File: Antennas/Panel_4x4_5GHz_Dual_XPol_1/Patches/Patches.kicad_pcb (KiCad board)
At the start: 2 copper layers, 186 x 226 mm, 92 parts

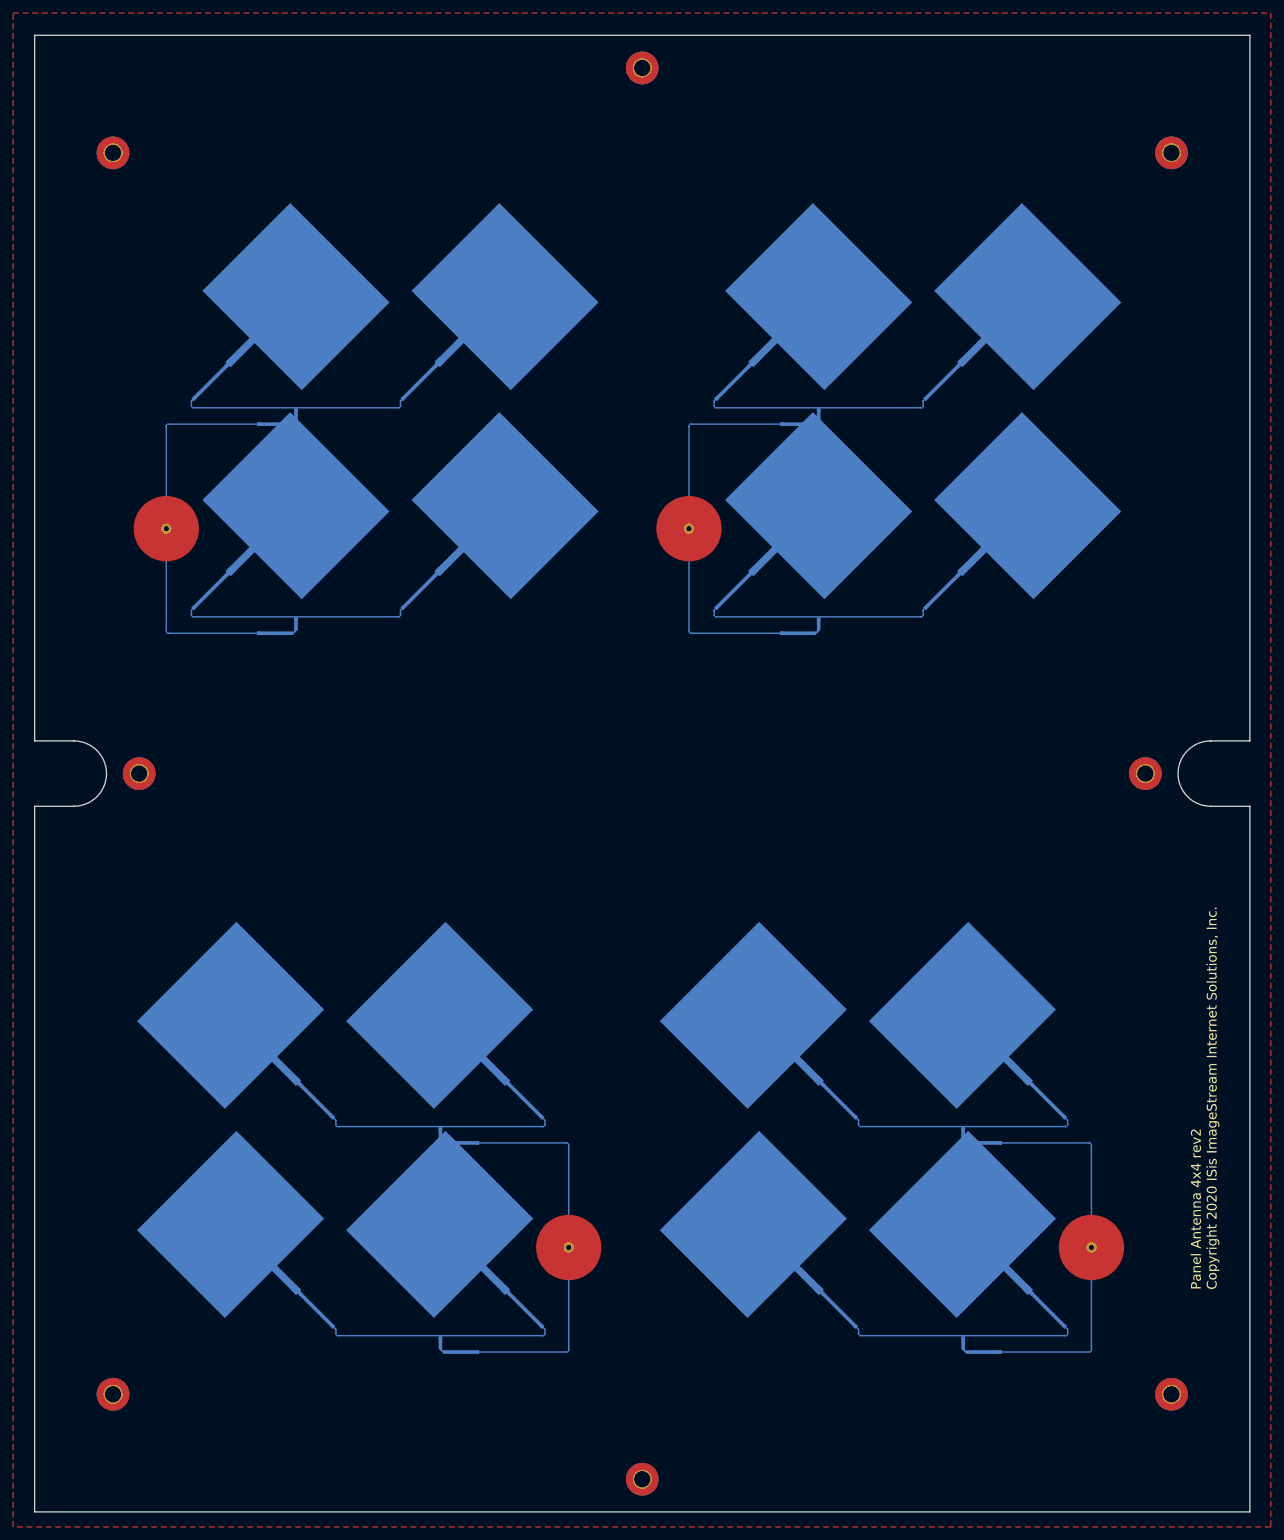
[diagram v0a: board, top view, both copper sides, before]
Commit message: Placed an order with JLCPCB for the Tighter 4pol version and the "Dual XPol" which actually was aperture coupled.
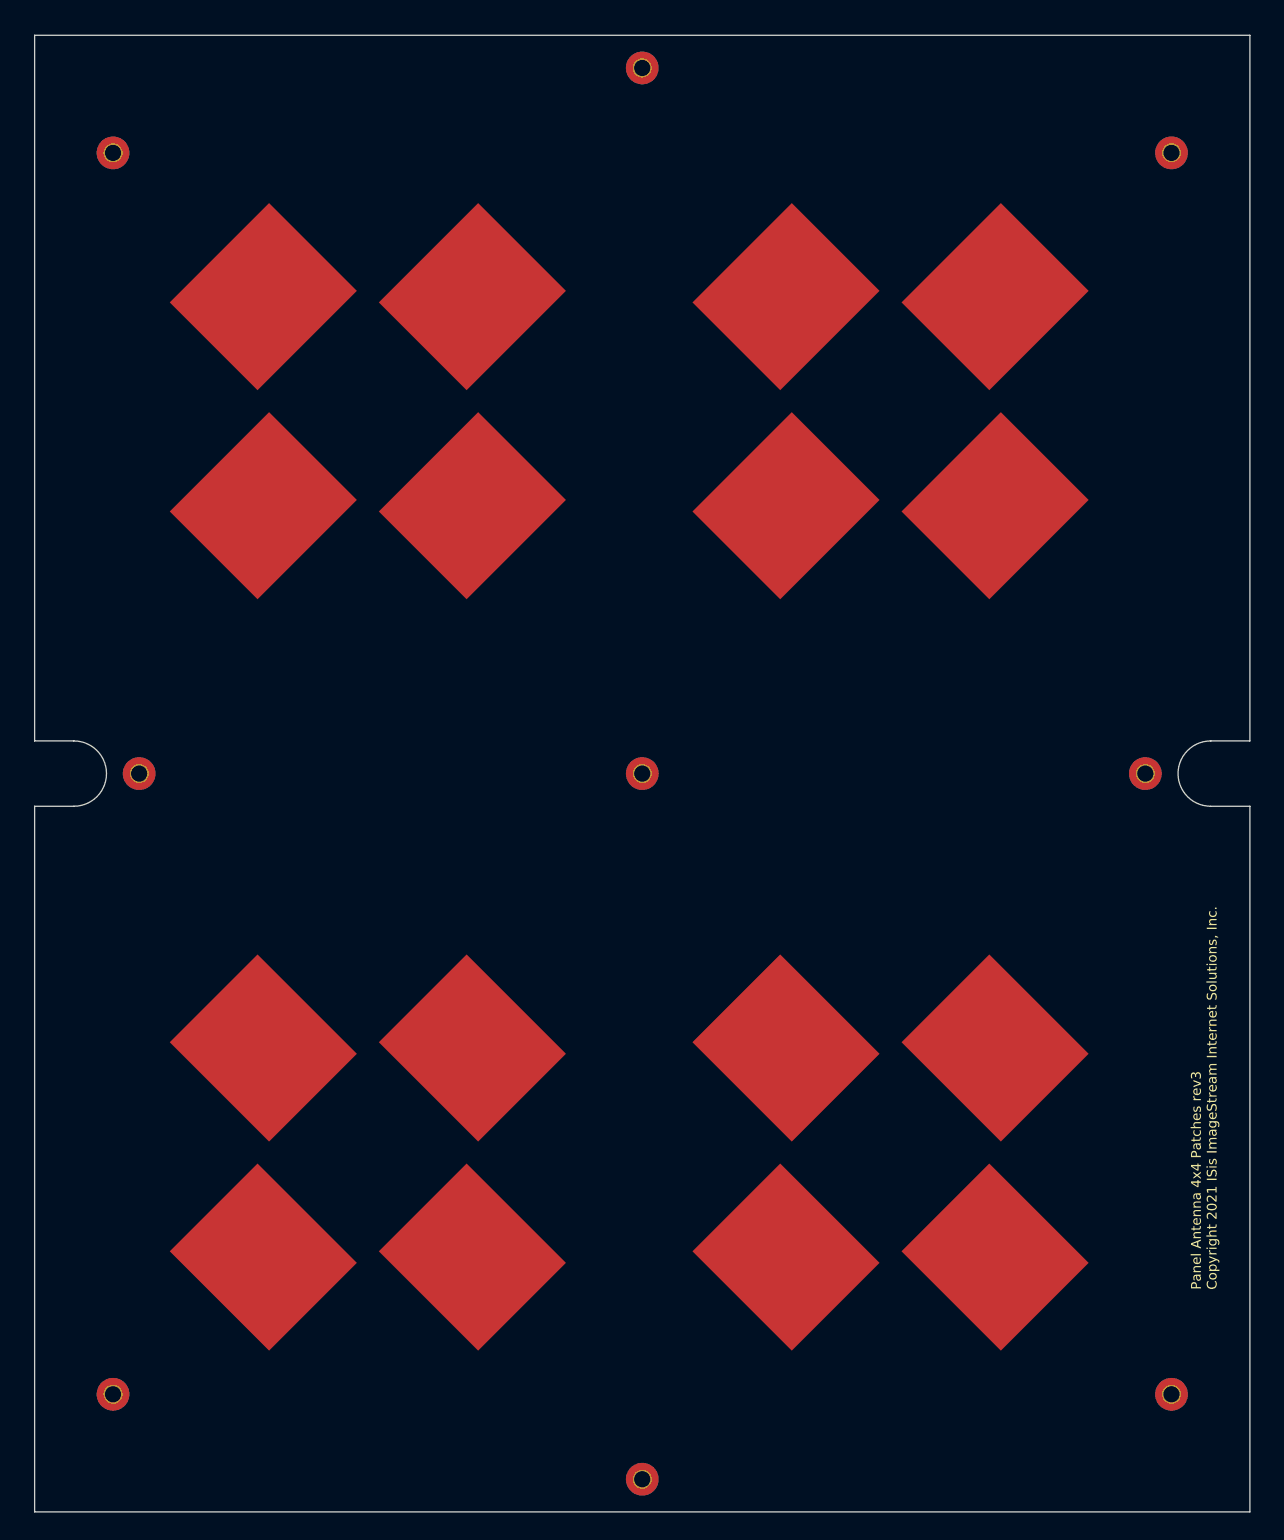
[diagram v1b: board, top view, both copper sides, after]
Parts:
- removed AE5 (x16): Antenna, Scott-RF-JLCPCB-600um7628-2layer:Feed_5.5_Linear_ApertureCoupled
- removed Feed1 (x4): Feed1, Scott:Flat_Ant_Hole
- removed the REF** at (78.1, 199.0)
- removed the REF** at (158.1, 167.0)
- removed the REF** at (40.0, 72.0)
- removed the REF** at (142.0, 150.0)
- removed the REF** at (104.0, 89.0)
- removed the REF** at (72.0, 40.0)
- removed the REF** at (142.1, 201.5)
- removed the REF** at (109.4, 82.6)
- removed the REF** at (152.6, 160.6)
- removed the REF** at (40.0, 59.5)
- removed the REF** at (56.0, 89.0)
- removed the REF** at (120.0, 72.0)
- removed the REF** at (24.0, 89.0)
- removed the REF** at (30.0, 182.0)
- removed the REF** at (142.1, 169.5)
- removed the REF** at (100.2, 91.5)
- removed the REF** at (40.6, 160.6)
- removed the REF** at (29.4, 50.6)
- removed the REF** at (126.1, 199.0)
- removed the REF** at (24.0, 57.0)
- removed the REF** at (62.0, 150.0)
- removed the REF** at (120.6, 160.6)
- removed the REF** at (161.7, 201.5)
- removed the REF** at (110.0, 182.0)
- removed the REF** at (40.0, 91.5)
- removed the REF** at (152.0, 40.0)
- removed the REF** at (62.0, 182.0)
- removed the REF** at (46.1, 199.0)
- removed the REF** at (161.7, 169.5)
- removed the REF** at (126.1, 167.0)
- removed the REF** at (40.0, 40.0)
- removed the REF** at (100.2, 59.5)
- removed the REF** at (81.7, 169.5)
- removed the REF** at (110.0, 150.0)
- removed the REF** at (120.0, 59.5)
- removed the REF** at (81.7, 201.5)
- removed the REF** at (30.0, 150.0)
- removed the REF** at (56.0, 57.0)
- removed the REF** at (20.2, 91.5)
- removed the REF** at (136.0, 57.0)
- removed the REF** at (109.4, 50.6)
- removed the REF** at (136.0, 89.0)
- removed the REF** at (152.6, 192.6)
- removed the REF** at (62.1, 169.5)
- removed the REF** at (104.0, 57.0)
- removed the REF** at (40.6, 192.6)
- removed the REF** at (141.4, 50.6)
- removed the REF** at (120.0, 40.0)
- removed the REF** at (120.0, 91.5)
- removed the REF** at (152.0, 72.0)
- removed the REF** at (61.4, 50.6)
- removed the REF** at (78.1, 167.0)
- removed the REF** at (72.6, 192.6)
- removed the REF** at (142.0, 182.0)
- removed the REF** at (72.0, 72.0)
- removed the REF** at (62.1, 201.5)
- removed the REF** at (141.4, 82.6)
- removed the REF** at (46.1, 167.0)
- removed the REF** at (29.4, 82.6)
- removed the REF** at (20.2, 59.5)
- removed the REF** at (72.6, 160.6)
- removed the REF** at (61.4, 82.6)
- removed the REF** at (158.1, 199.0)
- removed the REF** at (120.6, 192.6)
- added H11: Mounting Hole, MountingHole:MountingHole_2.5mm_Pad_TopBottom, F.Cu at (93.0, 113.0)
- added REF**: Patch_5.5_Linear_ApertureCoupled, Scott-RF-JLCPCB-600um7628-2layer:Patch_5.5_Linear_ApertureCoupled, F.Cu at (115.0, 187.0)
- added REF**: Patch_5.5_Linear_ApertureCoupled, Scott-RF-JLCPCB-600um7628-2layer:Patch_5.5_Linear_ApertureCoupled, F.Cu at (147.0, 187.0)
- added REF**: Patch_5.5_Linear_ApertureCoupled, Scott-RF-JLCPCB-600um7628-2layer:Patch_5.5_Linear_ApertureCoupled, F.Cu at (35.0, 155.0)
- added REF**: Patch_5.5_Linear_ApertureCoupled, Scott-RF-JLCPCB-600um7628-2layer:Patch_5.5_Linear_ApertureCoupled, F.Cu at (115.0, 72.0)
- added REF**: Patch_5.5_Linear_ApertureCoupled, Scott-RF-JLCPCB-600um7628-2layer:Patch_5.5_Linear_ApertureCoupled, F.Cu at (147.0, 40.0)
- added REF**: Patch_5.5_Linear_ApertureCoupled, Scott-RF-JLCPCB-600um7628-2layer:Patch_5.5_Linear_ApertureCoupled, F.Cu at (115.0, 40.0)
- added REF**: Patch_5.5_Linear_ApertureCoupled, Scott-RF-JLCPCB-600um7628-2layer:Patch_5.5_Linear_ApertureCoupled, F.Cu at (35.0, 187.0)
- added REF**: Patch_5.5_Linear_ApertureCoupled, Scott-RF-JLCPCB-600um7628-2layer:Patch_5.5_Linear_ApertureCoupled, F.Cu at (147.0, 155.0)
- added REF**: Patch_5.5_Linear_ApertureCoupled, Scott-RF-JLCPCB-600um7628-2layer:Patch_5.5_Linear_ApertureCoupled, F.Cu at (115.0, 155.0)
- added REF**: Patch_5.5_Linear_ApertureCoupled, Scott-RF-JLCPCB-600um7628-2layer:Patch_5.5_Linear_ApertureCoupled, F.Cu at (67.0, 72.0)
- added REF**: Patch_5.5_Linear_ApertureCoupled, Scott-RF-JLCPCB-600um7628-2layer:Patch_5.5_Linear_ApertureCoupled, F.Cu at (35.0, 72.0)
- added REF**: Patch_5.5_Linear_ApertureCoupled, Scott-RF-JLCPCB-600um7628-2layer:Patch_5.5_Linear_ApertureCoupled, F.Cu at (35.0, 40.0)
- added REF**: Patch_5.5_Linear_ApertureCoupled, Scott-RF-JLCPCB-600um7628-2layer:Patch_5.5_Linear_ApertureCoupled, F.Cu at (147.0, 72.0)
- added REF**: Patch_5.5_Linear_ApertureCoupled, Scott-RF-JLCPCB-600um7628-2layer:Patch_5.5_Linear_ApertureCoupled, F.Cu at (67.0, 155.0)
- added REF**: Patch_5.5_Linear_ApertureCoupled, Scott-RF-JLCPCB-600um7628-2layer:Patch_5.5_Linear_ApertureCoupled, F.Cu at (67.0, 40.0)
- added REF**: Patch_5.5_Linear_ApertureCoupled, Scott-RF-JLCPCB-600um7628-2layer:Patch_5.5_Linear_ApertureCoupled, F.Cu at (67.0, 187.0)
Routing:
- net /A1E3: track 250.9 -> 0.00 mm
- net (no net): track 129.4 -> 0.00 mm
- net /A1P1: track 125.2 -> 0.00 mm
- removed copper zone on F.Cu, net GND
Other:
- board text added: "Panel Antenna 4x4 Patches rev3 Copyright 2021 ISis ImageStream Internet Solutions, Inc."
- board text removed: "Panel Antenna 4x4 rev2 Copyright 2020 ISis ImageStream Internet Solutions, Inc."
